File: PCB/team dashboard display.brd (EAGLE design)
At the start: 160 x 100 mm, 36 parts, among them IC3 ICL7663CPA

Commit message: intial commit
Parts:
- moved U$8 21.6 mm to (62.2, 68.6)
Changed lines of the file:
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@@
 <attribute name="NAME" x="76.2" y="66.04" size="1.27" layer="25" rot="R90"/>
 </element>
-<element name="U$8" library="F-E library custom components" library_urn="urn:adsk.eagle:library:37896846" package="CAN_BUS" value="CAN_BUS" x="62.23" y="90.17" smashed="yes"/>
+<element name="U$8" library="F-E library custom components" library_urn="urn:adsk.eagle:library:37896846" package="CAN_BUS" value="CAN_BUS" x="62.23" y="68.58" smashed="yes"/>
 <element name="U$9" library="F-E library custom components" library_urn="urn:adsk.eagle:library:37896846" package="CAN_TEN" value="CAN_TEE" x="81.28" y="88.9" smashed="yes" rot="R270"/>
 </elements>

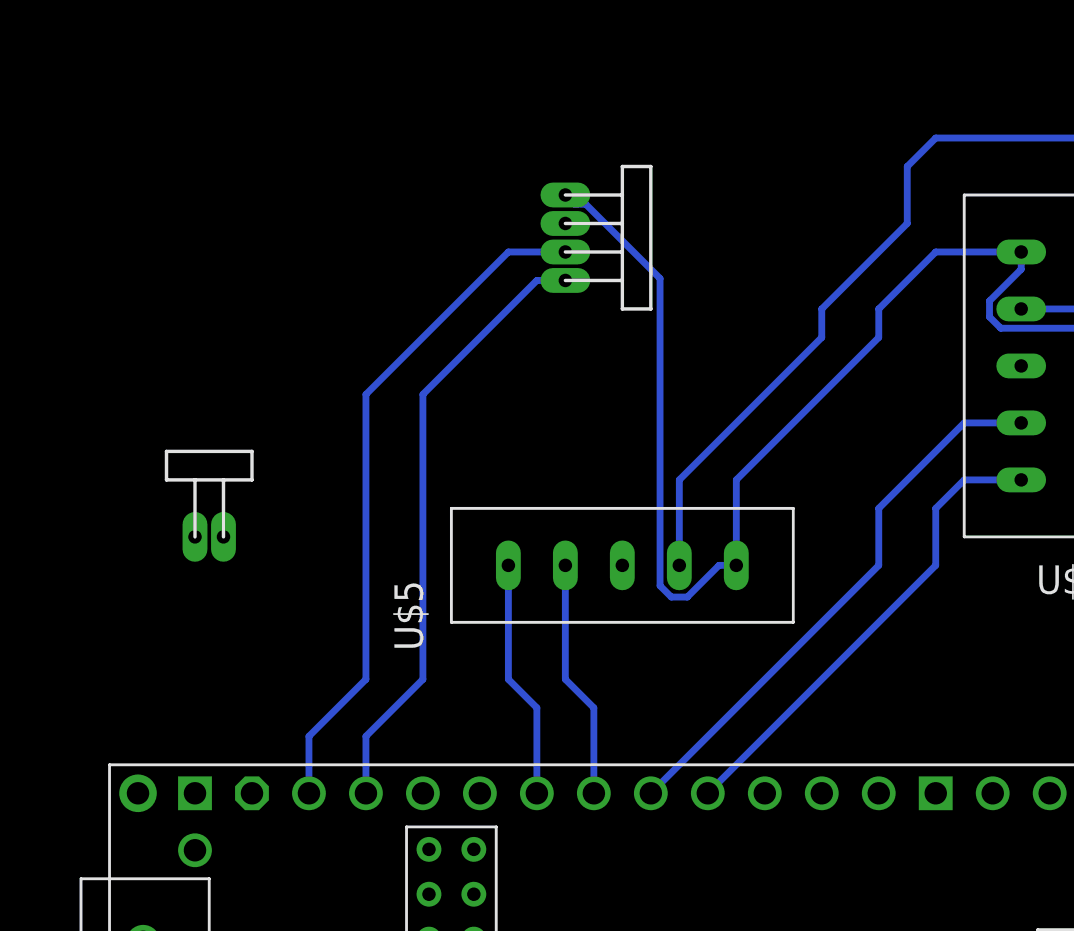
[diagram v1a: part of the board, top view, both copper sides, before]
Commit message: Stress board for Wheat bridge and edits
Created the Wheat bridge board with the different stress gauges in the F-E library. There were some minor edits that the other boards needed as well.
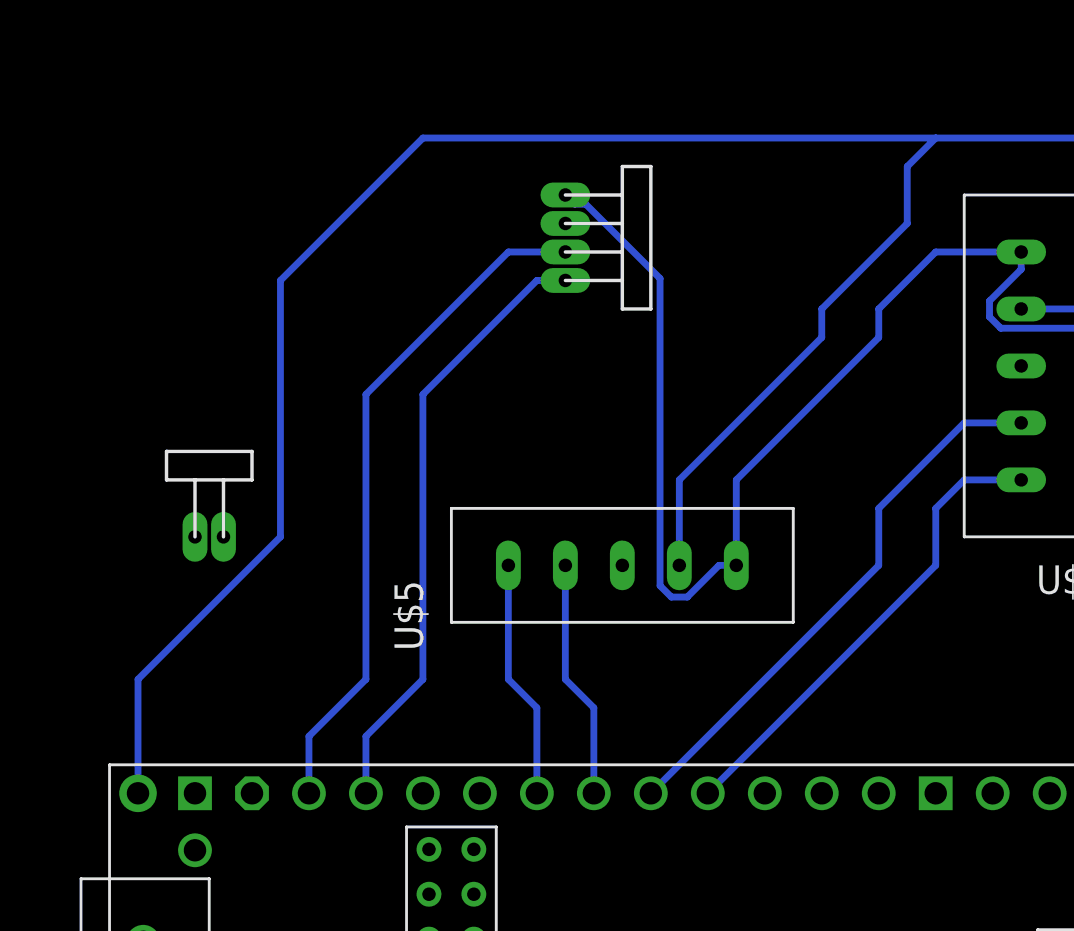
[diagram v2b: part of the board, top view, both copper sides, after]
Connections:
- net 5V: now also U$2.VIN
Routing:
- net 5V: track 50.3 -> 107.7 mm
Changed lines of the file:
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@@
 <wire x1="87.63" y1="69.85" x2="87.63" y2="73.66" width="0.3048" layer="16"/>
 <wire x1="113.03" y1="90.17" x2="107.95" y2="85.09" width="0.3048" layer="16"/>
+<contactref element="U$2" pad="VIN"/>
+<wire x1="63.5" y1="59.69" x2="63.5" y2="64.77" width="0.3048" layer="16"/>
+<wire x1="63.5" y1="64.77" x2="69.85" y2="71.12" width="0.3048" layer="16"/>
+<wire x1="69.85" y1="82.55" x2="76.2" y2="88.9" width="0.3048" layer="16"/>
+<wire x1="76.2" y1="88.9" x2="99.06" y2="88.9" width="0.3048" layer="16"/>
+<wire x1="69.85" y1="71.12" x2="69.85" y2="82.55" width="0.3048" layer="16"/>
 </signal>
 <signal name="N$6">
